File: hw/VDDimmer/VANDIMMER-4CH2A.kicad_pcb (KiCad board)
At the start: 4 copper layers, 100 x 84 mm, 98 parts, among them J1 USB-C 16P, J10 A2 V+SEL VIN/5V, J11 BTN1, J12 BTN2, J13 EXP 3V3/GND/SDA/SCL/EN/IO0, J14 UART1 3V3/GND/TX/RX, J2 VIN 12V, J3 CH1 LED-/V+, J4 CH2 LED-/V+, J5 CH3 LED-/V+, J6 CH4 LED-/V+, J7 ADDR1 V+/D/CLK/GND, J8 ADDR2 V+/D/CLK/GND, J9 A1 V+SEL VIN/5V, Q1 20N06, Q2 20N06, Q3 20N06, Q4 20N06, Q5 SUD50P06-15, U1 ESP32-S3-WROOM-1-N16R8, U2 AP63301WU-7, U3 BL1117-33CX, U4 74HCT125, U5 74HCT125

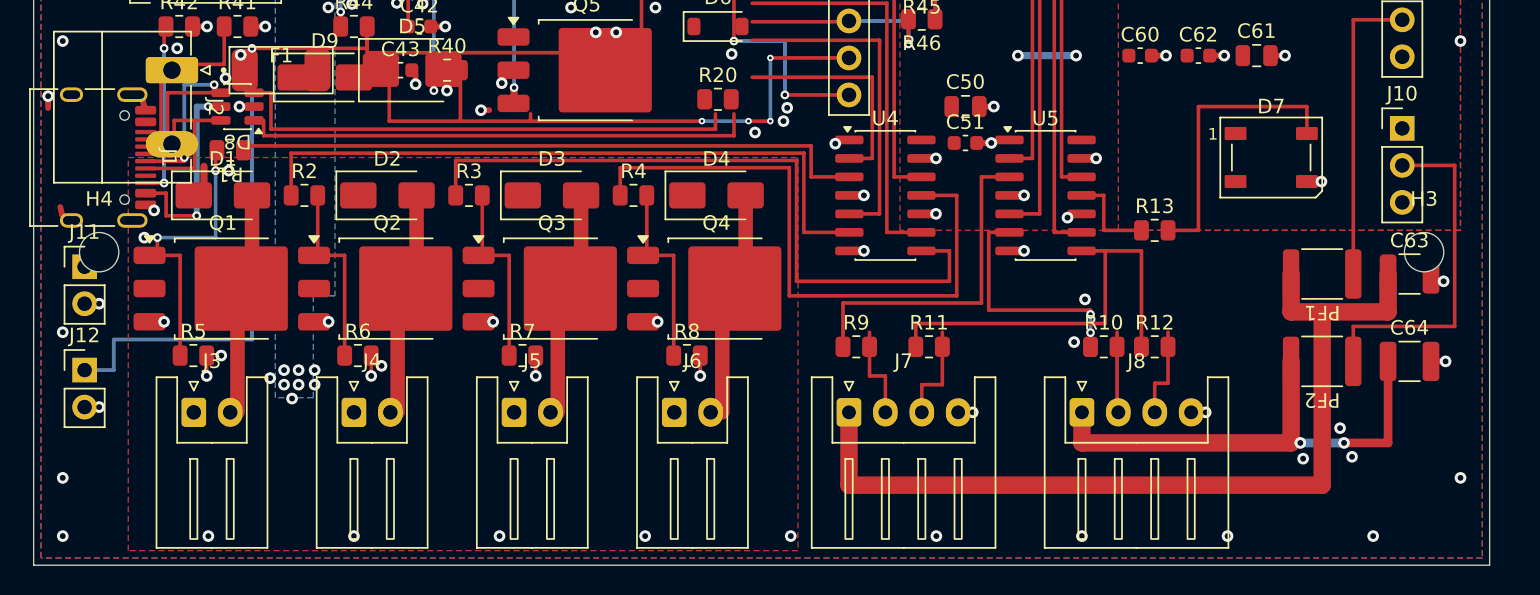
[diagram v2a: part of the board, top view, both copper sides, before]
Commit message: Place the harness row: 4 PWM, 2 addressable, USB-C on one face
All seven cable connectors now exit the bottom face - one harness, one gland,
one enclosure opening, per spec section 5. Placed against courtyards measured
from the live footprints (71.67 mm of bodies) rather than the plan's body
widths (71.04 mm), giving six uniform gaps of 4.05-4.06 mm inside 2.005 and
1.995 mm edge margins. Every connector's opening sits flush at y 139.245,
0.755 mm from the board edge.

J1 moves off the left edge to the far right of the harness face and rotates
-90 -> 0. Its through-hole shield pads are what blocked VIN_PROT from the left
edge on Rev A; that edge is now the 12 V input.

USB-to-antenna separation is 34.69 mm against the spec's 25-30 mm. Measured to
the antenna section itself (x 198.76..206.30, y 76.95..95.05, derived from the
F.Fab body outline beyond the outermost pad). A first measurement read 19.70 mm
because it used U1's courtyard bottom, which is the 48 mm keepout extent, not
the antenna - the courtyard is the wrong datum for this question. J1 also sits
entirely outside U1's keepout, which spans x 200.25..221.25 and is off-board.

fpspace.py reports 16 courtyard overlaps. Checked rather than eyeballed: zero
of them have both parts inside the Task 9/10 placed set - every one involves a
component Tasks 11/12 have yet to move. The courtyard gate becomes meaningful
at Task 12, which is where the plan puts it.

Co-Authored-By: Claude Opus 5 (1M context) <noreply@anthropic.com>
Claude-Session: https://claude.ai/code/session_01YZHVU8aymL4RkLeCfwomwj
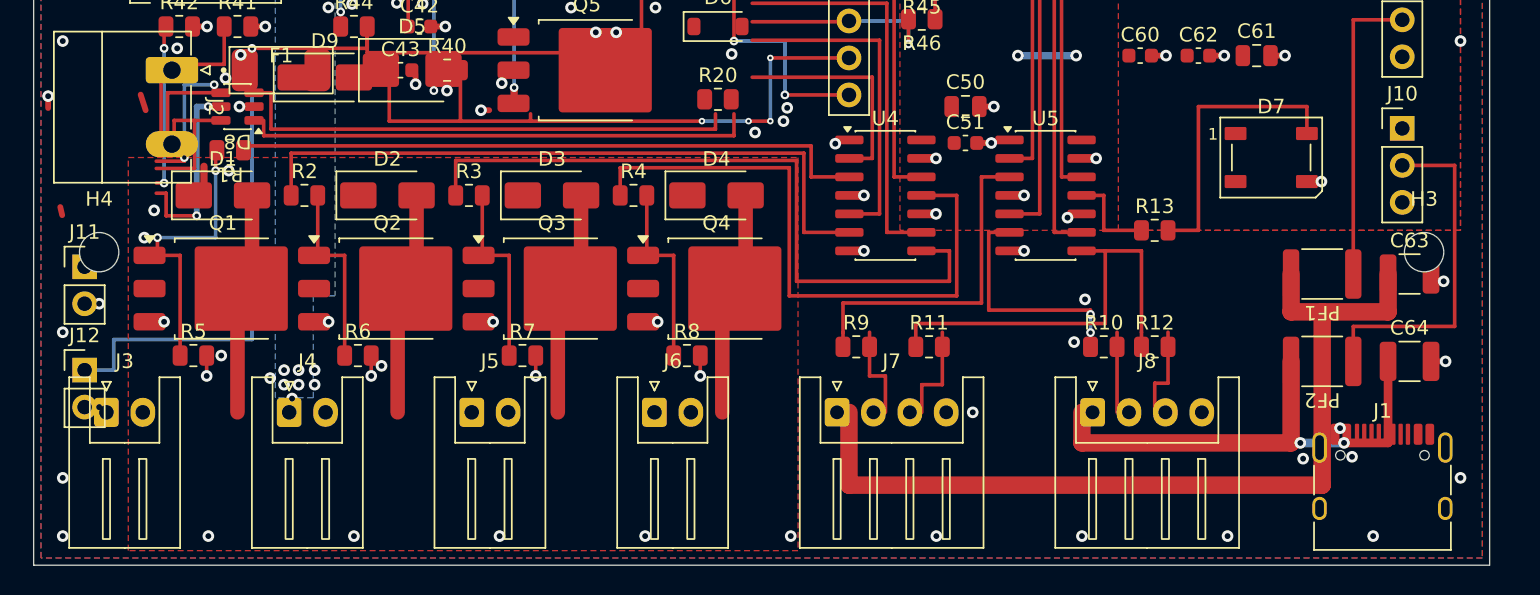
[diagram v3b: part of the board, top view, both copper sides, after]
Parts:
- moved J1 91.9 mm to (192.6, 135.1), turned to 0 degrees
- moved J3 6.00 mm to (105.0, 129.5)
- moved J4 4.45 mm to (117.5, 129.5)
- moved J5 2.91 mm to (130.1, 129.5)
- moved J6 1.36 mm to (142.6, 129.5)
- moved J7 0.82 mm to (155.2, 129.5)
- moved J8 0.73 mm to (172.7, 129.5)
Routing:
- net GND: vias 137 -> 136
- net /PWM/DRAIN2: vias 0 -> 1
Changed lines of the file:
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@@
 	(footprint "Connector_JST:JST_XH_S2B-XH-A_1x02_P2.50mm_Horizontal"
 		(layer "F.Cu")
-		(at 111 129.5)
+		(at 105 129.5)
 		(descr "JST XH series connector, S2B-XH-A (http://www.jst-mfg.com/product/pdf/eng/eXH.pdf)")
 		(tags "connector JST XH horizontal")
@@
 		(sheetname "/PWM/")
 		(sheetfile "PWM.kicad_sch")
-		(units
-			(unit
-				(name "A")
-				(pins "1" "2")
-			)
-		)
 		(duplicate_pad_numbers_are_jumpers no)
 		(fp_line
@@
 	(footprint "Connector_JST:JST_XH_S4B-XH-A_1x04_P2.50mm_Horizontal"
 		(layer "F.Cu")
-		(at 156 129.5)
+		(at 155.18 129.5)
 		(descr "JST XH series connector, S4B-XH-A (http://www.jst-mfg.com/product/pdf/eng/eXH.pdf)")
 		(tags "connector JST XH horizontal")
@@
 		(sheetname "/Addressable/")
 		(sheetfile "Addressable.kicad_sch")
-		(units
-			(unit
-				(name "A")
-				(pins "1" "2" "3" "4")
-			)
-		)
 		(duplicate_pad_numbers_are_jumpers no)
 		(fp_line
@@
 	(footprint "Connector_USB:USB_C_Receptacle_HRO_TYPE-C-31-M-12"
 		(layer "F.Cu")
-		(at 103.65 112 -90)
+		(at 192.64 135.05)
 		(descr "USB Type-C receptacle for USB 2.0 and PD, http://www.krhro.com/uploads/soft/180320/1-1P320120243.pdf")
 		(tags "usb usb-c 2.0 pd")
 		(property "Reference" "J1"
-			(at 0 -5.645 270)
+			(at 0 -5.645 0)
 			(unlocked yes)
 			(layer "F.SilkS")
@@
 		)
 		(property "Value" "USB-C 16P"
-			(at 0 5.1 270)
+			(at 0 5.1 0)
 			(unlocked yes)
 			(layer "F.SilkS")
@@
 		)
 		(property "Datasheet" ""
-			(at 0 0 90)
+			(at 0 0 180)
 			(layer "F.Fab")
 			(hide yes)
@@
 		)
 		(property "Description" ""
-			(at 0 0 90)
+			(at 0 0 180)
 			(layer "F.Fab")
 			(hide yes)
@@
 		)
 		(property "Assembly" "MACHINE-PLACED. SMD (surface mount, right angle) so it belongs in the SMT assembly, unlike J2-J14 which are through-hole and correctly hand-fit. 16 pads at 0.5 mm pitch plus four shell legs is not sensibly hand-soldered"
-			(at 0 0 270)
+			(at 0 0 0)
 			(unlocked yes)
 			(layer "F.Fab")
@@
 		)
 		(property "LCSC" "C165948"
-			(at 0 0 270)
+			(at 0 0 0)
 			(unlocked yes)
 			(layer "F.Fab")
@@
 		)
 		(property "MPN" "TYPE-C-31-M-12"
-			(at 0 0 270)
+			(at 0 0 0)
 			(unlocked yes)
 			(layer "F.Fab")
@@
 		)
 		(property "Manufacturer" "Korean Hroparts Elec"
-			(at 0 0 270)
+			(at 0 0 0)
 			(unlocked yes)
 			(layer "F.Fab")
@@
 		(sheetname "/MCU/")
 		(sheetfile "MCU.kicad_sch")
-		(units
-			(unit
-				(name "A")
-				(pins "SH" "A1" "A12" "B1" "B12" "A4" "A9" "B4" "B9" "A5" "B5" "A7" "B7"
-					"A6" "B6" "A8" "B8"
-				)
-			)
-		)
 		(duplicate_pad_numbers_are_jumpers no)
 		(fp_line
-			(start -4.7 3.9)
-			(end 4.7 3.9)
+			(start -4.7 -1.9)
+			(end -4.7 0.1)
 			(stroke
 				(width 0.12)
@@
 		)
 		(fp_line
-			(start 4.7 2)
+			(start -4.7 3.9)
 			(end 4.7 3.9)
 			(stroke
@@
 		)
 		(fp_line
-			(start -4.7 -1.9)
-			(end -4.7 0.1)
+			(start 4.7 -1.9)
+			(end 4.7 0.1)
 			(stroke
 				(width 0.12)
@@
 		)
 		(fp_line
-			(start 4.7 -1.9)
-			(end 4.7 0.1)
+			(start 4.7 2)
+			(end 4.7 3.9)
 			(stroke
 				(width 0.12)
@@
 		)
 		(fp_line
-			(start -5.32 4.15)
-			(end 5.32 4.15)
+			(start -5.32 -5.27)
+			(end -5.32 4.15)
 			(stroke
 				(width 0.05)
@@
 		(fp_line
 			(start -5.32 -5.27)
-			(end -5.32 4.15)
+			(end 5.32 -5.27)
 			(stroke
 				(width 0.05)
@@
 		)
 		(fp_line
-			(start -5.32 -5.27)
-			(end 5.32 -5.27)
+			(start -5.32 4.15)
+			(end 5.32 4.15)
 			(stroke
 				(width 0.05)
@@
 		)
 		(fp_line
-			(start -4.47 3.65)
-			(end 4.47 3.65)
+			(start -4.47 -3.65)
+			(end -4.47 3.65)
 			(stroke
 				(width 0.1)
@@
 		(fp_line
 			(start -4.47 -3.65)
-			(end -4.47 3.65)
+			(end 4.47 -3.65)
 			(stroke
 				(width 0.1)
@@
 		)
 		(fp_line
-			(start -4.47 -3.65)
-			(end 4.47 -3.65)
+			(start -4.47 3.65)
+			(end 4.47 3.65)
 			(stroke
 				(width 0.1)
@@
 		)
 		(fp_text user "${REFERENCE}"
-			(at 0 0 270)
+			(at 0 0 0)
 			(unlocked yes)
 			(layer "F.Fab")
@@
 		)
 		(pad "" np_thru_hole circle
-			(at -2.89 -2.6 270)
+			(at -2.89 -2.6)
 			(size 0.65 0.65)
 			(drill 0.65)
@@
 		)
 		(pad "" np_thru_hole circle
-			(at 2.89 -2.6 270)
+			(at 2.89 -2.6)
 			(size 0.65 0.65)
 			(drill 0.65)
@@
 		)
 		(pad "A1" smd roundrect
-			(at -3.25 -4.045 270)
+			(at -3.25 -4.045)
 			(size 0.6 1.45)
 			(layers "F.Cu" "F.Mask" "F.Paste")
@@
 		)
 		(pad "A4" smd roundrect
-			(at -2.45 -4.045 270)
+			(at -2.45 -4.045)
 			(size 0.6 1.45)
 			(layers "F.Cu" "F.Mask" "F.Paste")
@@
 		)
 		(pad "A5" smd roundrect
-			(at -1.25 -4.045 270)
+			(at -1.25 -4.045)
 			(size 0.3 1.45)
 			(layers "F.Cu" "F.Mask" "F.Paste")
@@
 		)
 		(pad "A6" smd roundrect
-			(at -0.25 -4.045 270)
+			(at -0.25 -4.045)
 			(size 0.3 1.45)
 			(layers "F.Cu" "F.Mask" "F.Paste")
@@
 		)
 		(pad "A7" smd roundrect
-			(at 0.25 -4.045 270)
+			(at 0.25 -4.045)
 			(size 0.3 1.45)
 			(layers "F.Cu" "F.Mask" "F.Paste")
@@
 		)
 		(pad "A8" smd roundrect
-			(at 1.25 -4.045 270)
+			(at 1.25 -4.045)
 			(size 0.3 1.45)
 			(layers "F.Cu" "F.Mask" "F.Paste")
@@
 		)
 		(pad "A9" smd roundrect
-			(at 2.45 -4.045 270)
+			(at 2.45 -4.045)
 			(size 0.6 1.45)
 			(layers "F.Cu" "F.Mask" "F.Paste")
@@
 		)
 		(pad "A12" smd roundrect
-			(at 3.25 -4.045 270)
+			(at 3.25 -4.045)
 			(size 0.6 1.45)
 			(layers "F.Cu" "F.Mask" "F.Paste")
@@
 		)
 		(pad "B1" smd roundrect
-			(at 3.25 -4.045 270)
+			(at 3.25 -4.045)
 			(size 0.6 1.45)
 			(layers "F.Cu" "F.Mask" "F.Paste")
@@
 		)
 		(pad "B4" smd roundrect
-			(at 2.45 -4.045 270)
+			(at 2.45 -4.045)
 			(size 0.6 1.45)
 			(layers "F.Cu" "F.Mask" "F.Paste")
@@
 		)
 		(pad "B5" smd roundrect
-			(at 1.75 -4.045 270)
+			(at 1.75 -4.045)
 			(size 0.3 1.45)
 			(layers "F.Cu" "F.Mask" "F.Paste")
@@
 		)
 		(pad "B6" smd roundrect
-			(at 0.75 -4.045 270)
+			(at 0.75 -4.045)
 			(size 0.3 1.45)
 			(layers "F.Cu" "F.Mask" "F.Paste")
@@
 		)
 		(pad "B7" smd roundrect
-			(at -0.75 -4.045 270)
+			(at -0.75 -4.045)
 			(size 0.3 1.45)
 			(layers "F.Cu" "F.Mask" "F.Paste")
@@
 		)
 		(pad "B8" smd roundrect
-			(at -1.75 -4.045 270)
+			(at -1.75 -4.045)
 			(size 0.3 1.45)
 			(layers "F.Cu" "F.Mask" "F.Paste")
@@
 		)
 		(pad "B9" smd roundrect
-			(at -2.45 -4.045 270)
+			(at -2.45 -4.045)
 			(size 0.6 1.45)
 			(layers "F.Cu" "F.Mask" "F.Paste")
@@
 		)
 		(pad "B12" smd roundrect
-			(at -3.25 -4.045 270)
+			(at -3.25 -4.045)
 			(size 0.6 1.45)
 			(layers "F.Cu" "F.Mask" "F.Paste")
@@
 		)
 		(pad "SH" thru_hole oval
-			(at -4.32 -3.13 270)
+			(at -4.32 -3.13)
 			(size 1 2.1)
 			(drill oval 0.6 1.7)
@@
 		)
 		(pad "SH" thru_hole oval
-			(at -4.32 1.05 270)
+			(at -4.32 1.05)
 			(size 1 1.6)
 			(drill oval 0.6 1.2)
@@
 		)
 		(pad "SH" thru_hole oval
-			(at 4.32 -3.13 270)
+			(at 4.32 -3.13)
 			(size 1 2.1)
 			(drill oval 0.6 1.7)
@@
 		)
 		(pad "SH" thru_hole oval
-			(at 4.32 1.05 270)
+			(at 4.32 1.05)
 			(size 1 1.6)
 			(drill oval 0.6 1.2)
@@
 	(footprint "Connector_JST:JST_XH_S4B-XH-A_1x04_P2.50mm_Horizontal"
 		(layer "F.Cu")
-		(at 172 129.5)
+		(at 172.73 129.5)
 		(descr "JST XH series connector, S4B-XH-A (http://www.jst-mfg.com/product/pdf/eng/eXH.pdf)")
 		(tags "connector JST XH horizontal")
@@
 		(sheetname "/Addressable/")
 		(sheetfile "Addressable.kicad_sch")
-		(units
-			(unit
-				(name "A")
-				(pins "1" "2" "3" "4")
-			)
-		)
 		(duplicate_pad_numbers_are_jumpers no)
 		(fp_line
@@
 	(footprint "Connector_JST:JST_XH_S2B-XH-A_1x02_P2.50mm_Horizontal"
 		(layer "F.Cu")
-		(at 144 129.5)
+		(at 142.64 129.5)
 		(descr "JST XH series connector, S2B-XH-A (http://www.jst-mfg.com/product/pdf/eng/eXH.pdf)")
 		(tags "connector JST XH horizontal")
@@
 		(sheetname "/PWM/")
 		(sheetfile "PWM.kicad_sch")
-		(units
-			(unit
-				(name "A")
-				(pins "1" "2")
-			)
-		)
 		(duplicate_pad_numbers_are_jumpers no)
 		(fp_line
@@
 	(footprint "Connector_JST:JST_XH_S2B-XH-A_1x02_P2.50mm_Horizontal"
 		(layer "F.Cu")
-		(at 122 129.5)
+		(at 117.55 129.5)
 		(descr "JST XH series connector, S2B-XH-A (http://www.jst-mfg.com/product/pdf/eng/eXH.pdf)")
 		(tags "connector JST XH horizontal")
@@
 		(sheetname "/PWM/")
 		(sheetfile "PWM.kicad_sch")
-		(units
-			(unit
-				(name "A")
-				(pins "1" "2")
-			)
-		)
 		(duplicate_pad_numbers_are_jumpers no)
 		(fp_line
@@
 	(footprint "Connector_JST:JST_XH_S2B-XH-A_1x02_P2.50mm_Horizontal"
 		(layer "F.Cu")
-		(at 133 129.5)
+		(at 130.09 129.5)
 		(descr "JST XH series connector, S2B-XH-A (http://www.jst-mfg.com/product/pdf/eng/eXH.pdf)")
 		(tags "connector JST XH horizontal")
@@
 		(sheetname "/PWM/")
 		(sheetfile "PWM.kicad_sch")
-		(units
-			(unit
-				(name "A")
-				(pins "1" "2")
-			)
-		)
 		(duplicate_pad_numbers_are_jumpers no)
 		(fp_line
@@
 	)
 	(via
-		(at 117.75 128.553)
-		(size 0.8)
-		(drill 0.4)
-		(layers "F.Cu" "B.Cu")
-		(net "GND")
-	)
-	(via
 		(at 136.678 100.482)
 		(size 0.8)
@@
 		(net "/PWM/DRAIN2")
 	)
+	(via
+		(at 117.75 128.553)
+		(size 0.8)
+		(drill 0.4)
+		(layers "F.Cu" "B.Cu")
+		(net "/PWM/DRAIN2")
+	)

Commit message: Place MCU region, level shifters and the human interface
J11, J12 and D7 move to the top face as one group - press and watch is a
single interaction sharing one panel cutout, per spec section 5.

J13 and J14 sit at x 174.19..177.81, immediately left of U1, keeping the
expansion signals (SDA/SCL/EN/BOOT, TX/RX) about 3 mm from the module pads.
J14 also rotates 90 -> 0 so both headers stack vertically.

PF1/PF2 and J9/J10 group above J7/J8 with the addressable outputs they feed.

The governing constraint here is one the plan does not mention: U1's courtyard
is 41.25 x 48.05 mm because it encloses the whole antenna keepout, so on-board
it occupies x 180.00..200, y 61.95..110.05 - far more than the 18.1 mm-tall
module body. This project grades courtyards_overlap as an ERROR, so that strip
is unusable for components and everything on the right side must clear it. The
library courtyard is left intact rather than trimmed to the body: editing a
placed instance's courtyard would diverge it from the library silently, and
lib_footprint_mismatch is already noisy on this board.

J9/J10 therefore stack in the 19.69 mm band between U1's courtyard bottom
(110.05) and J1's top (129.74). A first attempt left J9 only 0.14 mm off the
courtyard - too thin to survive rounding - so the pair was retightened to
0.74 / 0.79 / 0.74 mm clearances through the chain.

fpspace.py: 13 overlaps, down from 16. Verified programmatically that none has
both parts inside the placed set; every one still involves a Task 12 component.

Co-Authored-By: Claude Opus 5 (1M context) <noreply@anthropic.com>
Claude-Session: https://claude.ai/code/session_01YZHVU8aymL4RkLeCfwomwj
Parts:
- moved D7 73.6 mm to (132.0, 61.0)
- moved J12 68.4 mm to (119.0, 60.0)
- moved J14 68.0 mm to (176.0, 98.0), turned to 0 degrees
- moved J11 60.1 mm to (112.0, 60.0)
- moved J13 25.0 mm to (176.0, 80.0)
- moved J9 14.0 mm to (188.0, 112.6)
- moved J10 13.5 mm to (188.0, 122.1)
- moved PF1 11.0 mm to (180.0, 113.0)
- moved PF2 10.4 mm to (180.0, 120.0)
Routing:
- net /MCU/UART1_TX: track 33.3 -> 0.00 mm
- net +5V: track 75.8 -> 109.0 mm
- net GND: track 27.9 -> 55.7 mm, vias 136 -> 134
- net /Power/VIN_FUSED: track 27.8 -> 0.00 mm
- net /Power/QREV_G: track 25.6 -> 49.6 mm, vias 0 -> 2
- net /MCU/BOOT_IO0: track 26.3 -> 2.30 mm, vias 2 -> 0
- net VIN_PROT: vias 14 -> 15
- net /PWM/DRAIN1: vias 0 -> 1
